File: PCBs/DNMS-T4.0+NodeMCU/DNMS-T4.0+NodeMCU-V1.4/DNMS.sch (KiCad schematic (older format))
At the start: 12 parts, among them J1 Conn_02x03_Odd_Even, J2 Conn_01x02, J3 Conn_01x04, J4 Conn_01x05, U1 NodeMCU V2, U2 NodeMCU V3, U3 Teensy4.0

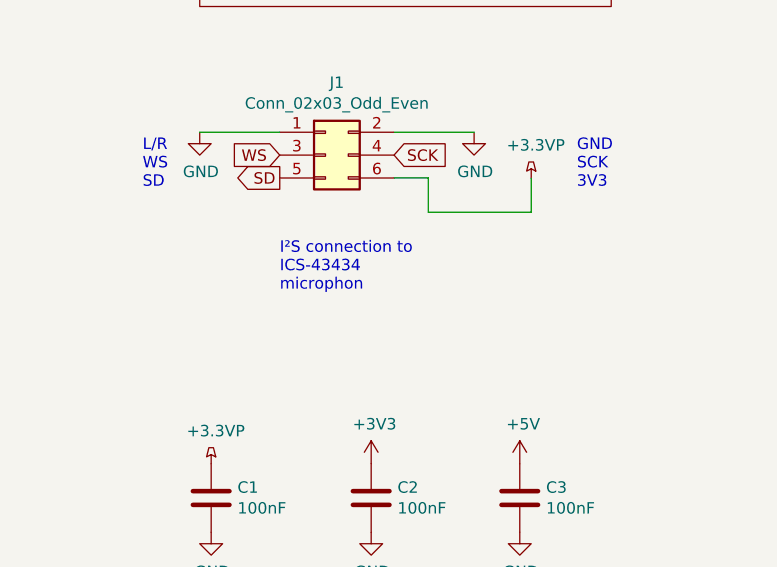
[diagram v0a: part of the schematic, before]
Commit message: spelling changes
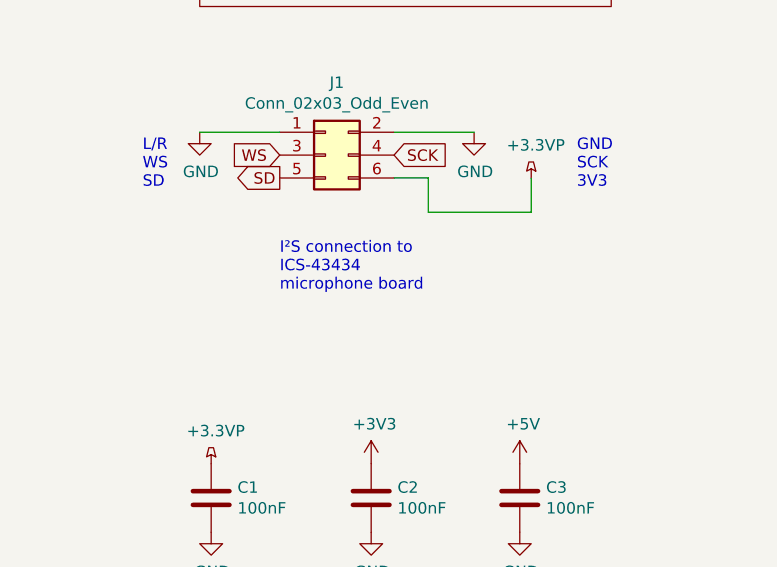
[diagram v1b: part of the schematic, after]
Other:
- note added: "I²S connection to\nICS-43434\nmicrophone board"
- note removed: "I²S connection to\nICS-43434\nmicrophon"
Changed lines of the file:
@@
 L/R\nWS\nSD
 Text Notes 1950 5150 0    50   ~ 0
-I²S connection to\nICS-43434\nmicrophon
+I²S connection to\nICS-43434\nmicrophone board
 Text Notes 3250 4700 0    50   ~ 0
 GND\nSCK\n3V3
